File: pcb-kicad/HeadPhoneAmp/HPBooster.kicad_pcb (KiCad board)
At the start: 2 copper layers, 64.1 x 37 mm, 36 parts, among them J1 Conn_01x03, J2 AudioJack3, J3 Conn_01x02_Socket, U5 TPA6120A2RGY

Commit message: Added some order infos.
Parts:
- J3: value Conn_01x02_Socket -> ~
- U1: value ~ -> TPS65135
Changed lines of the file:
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@@
 		(tags "resistor handsolder")
 		(property "Reference" "R39"
-			(at 0 -1.43 360)
+			(at 0 -1.43 0)
 			(layer "F.SilkS")
 			(effects
@@
 		)
 		(property "Value" "1k"
-			(at 0 1.43 360)
+			(at 0 1.43 0)
 			(layer "F.Fab")
 			(effects
@@
 		)
 		(fp_text user "${REFERENCE}"
-			(at 0 0 360)
+			(at 0 0 0)
 			(layer "F.Fab")
 			(effects
@@
 		(tags "resistor handsolder")
 		(property "Reference" "R37"
-			(at 0 -1.43 360)
+			(at 0 -1.43 0)
 			(layer "F.SilkS")
 			(effects
@@
 		)
 		(property "Value" "1k"
-			(at 0 1.43 360)
+			(at 0 1.43 0)
 			(layer "F.Fab")
 			(effects
@@
 		)
 		(fp_text user "${REFERENCE}"
-			(at 0 0 360)
+			(at 0 0 0)
 			(layer "F.Fab")
 			(effects
@@
 		(tags "connector JST EH vertical")
 		(property "Reference" "J1"
-			(at -4.4088 -0.0048 360)
+			(at -4.4088 -0.0048 0)
 			(layer "F.SilkS")
 			(hide yes)
@@
 		)
 		(property "Value" "Conn_01x03"
-			(at 2.5 3.4 360)
+			(at 2.5 3.4 0)
 			(layer "F.Fab")
 			(hide yes)
@@
 		)
 		(fp_text user "${REFERENCE}"
-			(at 2.5 1.5 360)
+			(at 2.5 1.5 0)
 			(layer "F.Fab")
 			(effects
@@
 		(tags "resistor handsolder")
 		(property "Reference" "R7"
-			(at 2.6924 0.1524 360)
+			(at 2.6924 0.1524 0)
 			(layer "F.SilkS")
 			(effects
@@
 		)
 		(property "Value" "487k"
-			(at 0 1.43 360)
+			(at 0 1.43 0)
 			(layer "F.Fab")
 			(effects
@@
 		)
 		(fp_text user "${REFERENCE}"
-			(at 0 0 360)
+			(at 0 0 0)
 			(layer "F.Fab")
 			(effects
@@
 		(tags "resistor handsolder")
 		(property "Reference" "R6"
-			(at 2.8916 0.0628 360)
+			(at 2.8916 0.0628 0)
 			(layer "F.SilkS")
 			(effects
@@
 		)
 		(property "Value" "120k"
-			(at 0 1.43 360)
+			(at 0 1.43 0)
 			(layer "F.Fab")
 			(effects
@@
 		)
 		(fp_text user "${REFERENCE}"
-			(at 0 0 360)
+			(at 0 0 0)
 			(layer "F.Fab")
 			(effects
@@
 		(tags "capacitor handsolder")
 		(property "Reference" "C2"
-			(at -2.8702 -0.0762 360)
+			(at -2.8702 -0.0762 0)
 			(layer "F.SilkS")
 			(effects
@@
 		)
 		(property "Value" "100n"
-			(at 0 1.43 360)
+			(at 0 1.43 0)
 			(layer "F.Fab")
 			(effects
@@
 		)
 		(fp_text user "${REFERENCE}"
-			(at 0 0 360)
+			(at 0 0 0)
 			(layer "F.Fab")
 			(effects
@@
 		(tags "capacitor handsolder")
 		(property "Reference" "C43"
-			(at 0 -1.43 360)
+			(at 0 -1.43 0)
 			(layer "F.SilkS")
 			(effects
@@
 		)
 		(property "Value" "100n"
-			(at 0 1.43 360)
+			(at 0 1.43 0)
 			(layer "F.Fab")
 			(effects
@@
 		)
 		(fp_text user "${REFERENCE}"
-			(at 0 0 360)
+			(at 0 0 0)
 			(layer "F.Fab")
 			(effects
@@
 		(tags "capacitor handsolder")
 		(property "Reference" "C3"
-			(at 2.6416 0.0508 360)
+			(at 2.6416 0.0508 0)
 			(layer "F.SilkS")
 			(effects
@@
 		)
 		(property "Value" "100n"
-			(at 0 1.43 360)
+			(at 0 1.43 0)
 			(layer "F.Fab")
 			(effects
@@
 		)
 		(fp_text user "${REFERENCE}"
-			(at 0 0 360)
+			(at 0 0 0)
 			(layer "F.Fab")
 			(effects
@@
 			)
 		)
-		(property "Value" "Conn_01x02_Socket"
+		(property "Value" "~"
 			(at 0 4.87 0)
 			(layer "F.Fab")
@@
 			)
 		)
-		(property "Value" "~"
+		(property "Value" "TPS65135"
 			(at 0 2.83 45)
 			(layer "F.Fab")
@@
 		(tags "capacitor handsolder")
 		(property "Reference" "C4"
-			(at 2.7646 0.0628 360)
+			(at 2.7646 0.0628 0)
 			(layer "F.SilkS")
 			(effects
@@
 		)
 		(property "Value" "10u"
-			(at 0 1.43 360)
+			(at 0 1.43 0)
 			(layer "F.Fab")
 			(effects
@@
 		)
 		(fp_text user "${REFERENCE}"
-			(at 0 0 360)
+			(at 0 0 0)
 			(layer "F.Fab")
 			(effects
@@
 		(tags "inductor handsolder")
 		(property "Reference" "FB1"
-			(at -3.2332 -0.0374 360)
+			(at -3.2332 -0.0374 0)
 			(layer "F.SilkS")
 			(effects
@@
 		)
 		(property "Value" "FerriteBead"
-			(at 0 1.43 360)
+			(at 0 1.43 0)
 			(layer "F.Fab")
 			(hide yes)
@@
 		)
 		(fp_text user "${REFERENCE}"
-			(at 0 0 360)
+			(at 0 0 0)
 			(layer "F.Fab")
 			(effects
@@
 		(tags "resistor handsolder")
 		(property "Reference" "R38"
-			(at 0 -1.43 360)
+			(at 0 -1.43 0)
 			(layer "F.SilkS")
 			(effects
@@
 		)
 		(property "Value" "1k"
-			(at 0 1.43 360)
+			(at 0 1.43 0)
 			(layer "F.Fab")
 			(effects
@@
 		)
 		(fp_text user "${REFERENCE}"
-			(at 0 0 360)
+			(at 0 0 0)
 			(layer "F.Fab")
 			(effects
@@
 		(tags "resistor handsolder")
 		(property "Reference" "R36"
-			(at 0 -1.43 360)
+			(at 0 -1.43 0)
 			(layer "F.SilkS")
 			(effects
@@
 		)
 		(property "Value" "1k"
-			(at 0 1.43 360)
+			(at 0 1.43 0)
 			(layer "F.Fab")
 			(effects
@@
 		)
 		(fp_text user "${REFERENCE}"
-			(at 0 0 360)
+			(at 0 0 0)
 			(layer "F.Fab")
 			(effects
@@
 		(tags "capacitor handsolder")
 		(property "Reference" "C5"
-			(at -2.6376 -0.0628 360)
+			(at -2.6376 -0.0628 0)
 			(layer "F.SilkS")
 			(effects
@@
 		)
 		(property "Value" "10u"
-			(at 0 1.43 360)
+			(at 0 1.43 0)
 			(layer "F.Fab")
 			(effects
@@
 		)
 		(fp_text user "${REFERENCE}"
-			(at 0 0 360)
+			(at 0 0 0)
 			(layer "F.Fab")
 			(effects
@@
 		(tags "capacitor handsolder")
 		(property "Reference" "C1"
-			(at -2.9718 -0.0762 360)
+			(at -2.9718 -0.0762 0)
 			(layer "F.SilkS")
 			(effects
@@
 		)
 		(property "Value" "10u"
-			(at 0 1.43 360)
+			(at 0 1.43 0)
 			(layer "F.Fab")
 			(effects
@@
 		)
 		(fp_text user "${REFERENCE}"
-			(at 0 0 360)
+			(at 0 0 0)
 			(layer "F.Fab")
 			(effects
@@
 		(tags "resistor handsolder")
 		(property "Reference" "R1"
-			(at 2.8408 0.012 360)
+			(at 2.8408 0.012 0)
 			(layer "F.SilkS")
 			(effects
@@
 		)
 		(property "Value" "365k"
-			(at 0 1.43 360)
+			(at 0 1.43 0)
 			(layer "F.Fab")
 			(effects
@@
 		)
 		(fp_text user "${REFERENCE}"
-			(at 0 0 360)
+			(at 0 0 0)
 			(layer "F.Fab")
 			(effects

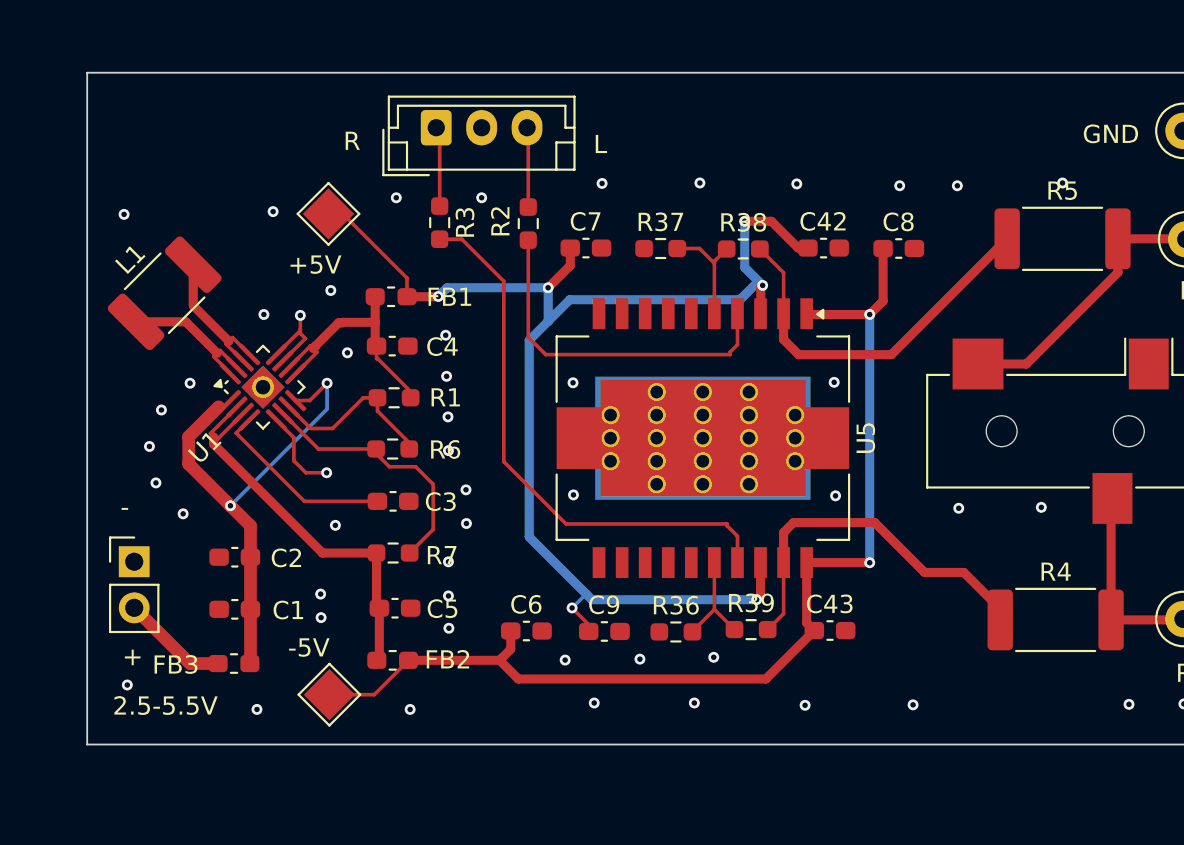
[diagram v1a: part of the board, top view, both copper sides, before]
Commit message: HPBooster v0.2, changed TPA footprint.
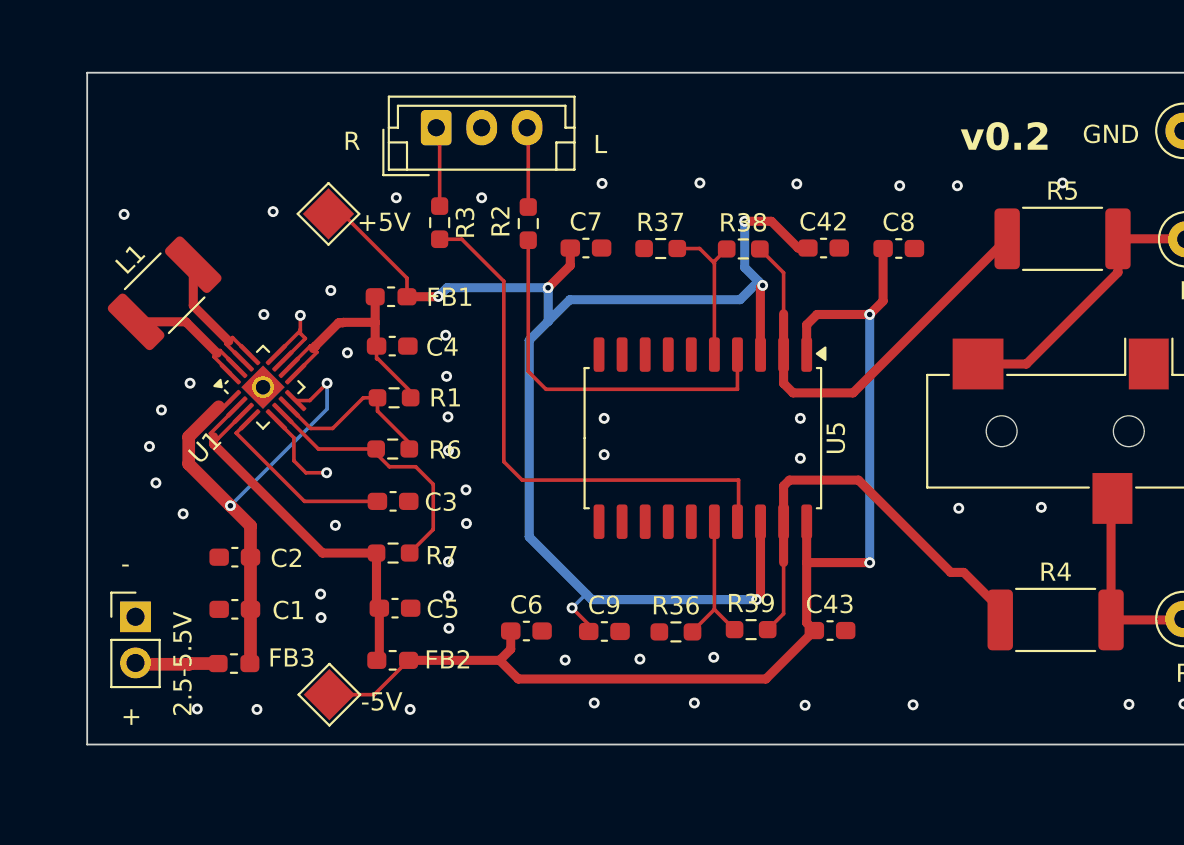
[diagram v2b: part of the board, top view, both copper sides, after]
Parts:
- J1: value Conn_01x03 -> ~
- J2: value AudioJack3 -> ~
- TP1, TP2, TP3, TP5+1, TP5-1: value TestPoint -> ~
- U5: footprint Package_SO:HSOP-20-1EP_11.0x15.9mm_P1.27mm_SlugDown_ThermalVias -> Package_SO:SOP-20_7.5x12.8mm_P1.27mm
- moved J3 3.03 mm to (103.6, 123.5)
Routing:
- net +6HPV: track 72.6 -> 77.1 mm
- net -6HPV: track 59.4 -> 63.5 mm
- net Net-(R39-Pad2): track 20.4 -> 23.9 mm
- net Net-(R38-Pad2): track 20.8 -> 24.0 mm
- net Net-(U5B--): track 5.89 -> 8.14 mm
- net Net-(U5A--): track 6.23 -> 8.48 mm
- net Net-(U5A-+): track 19.3 -> 21.1 mm
- net +5V: track 5.89 -> 4.63 mm
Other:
- board text added: "v0.2"
